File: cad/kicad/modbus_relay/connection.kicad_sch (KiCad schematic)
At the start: 11 parts, among them J11 Screw_Terminal_01x02, J2 Screw_Terminal_01x03, J4 Screw_Terminal_01x02, J5 Screw_Terminal_01x03, J6 Screw_Terminal_01x03, J7 Screw_Terminal_01x03, J8 Screw_Terminal_01x03, J9 Screw_Terminal_01x02

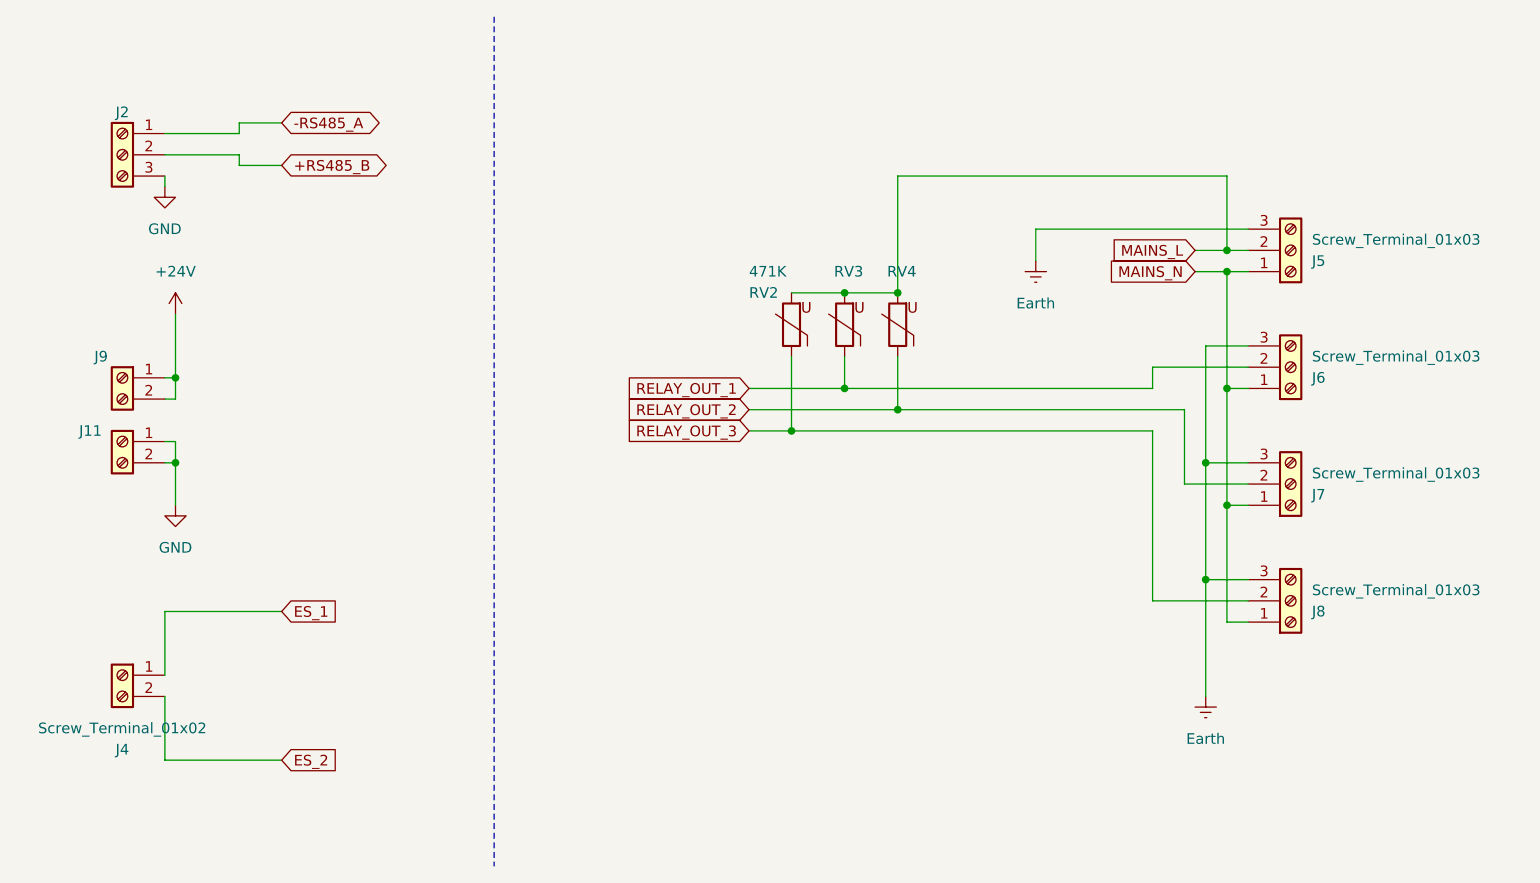
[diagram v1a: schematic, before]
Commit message: Double sided version
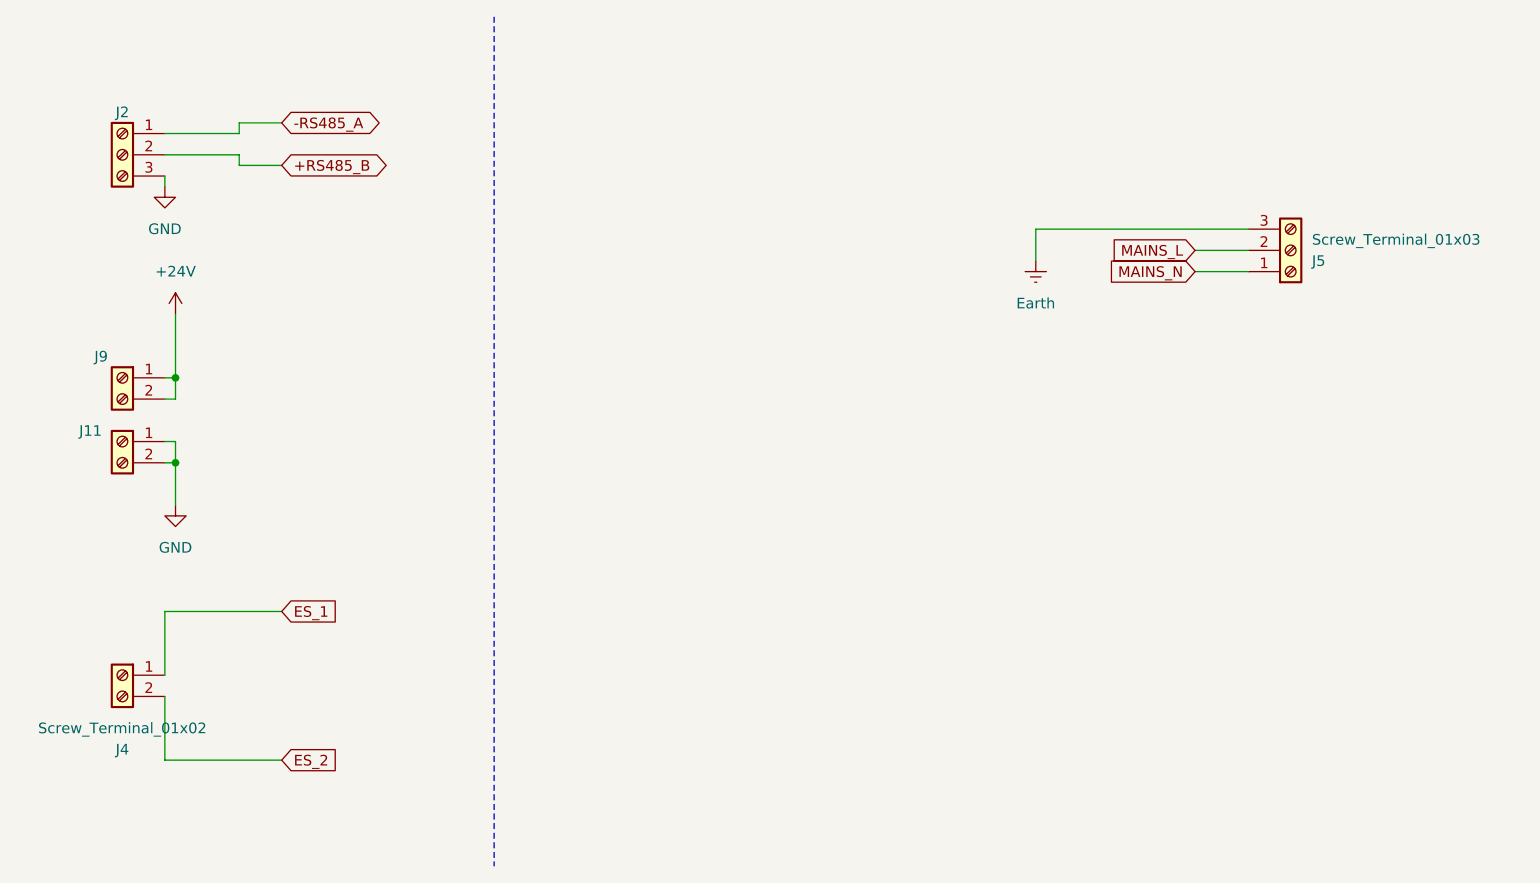
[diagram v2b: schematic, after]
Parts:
- removed J6, J7, J8: Screw_Terminal_01x03, Connector_Phoenix_MSTB:PhoenixContact_MSTBVA_2,5_3-G-5,08_1x03_P5.08mm_Vertical, symbol Connector:Screw_Terminal_01x03
- removed RV2, RV3, RV4: 471K, adarwoo:MOV471, symbol Device:Varistor
